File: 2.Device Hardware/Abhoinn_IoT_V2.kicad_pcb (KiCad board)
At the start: 4 copper layers, 46 parts, among them IC1 AX-SIP-SFEU-1-01-TX30, IC2 MS5840-02BA01, J1 Conn_01x02, J2 Conn_01x02, J3 Conn_02x05_Odd_Even, J4 Conn_02x05_Odd_Even, J5 Conn_Coaxial, J6 Conn_01x02_Female, P1 USB_C_Plug_USB2.0, U1 XC6206PxxxMR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

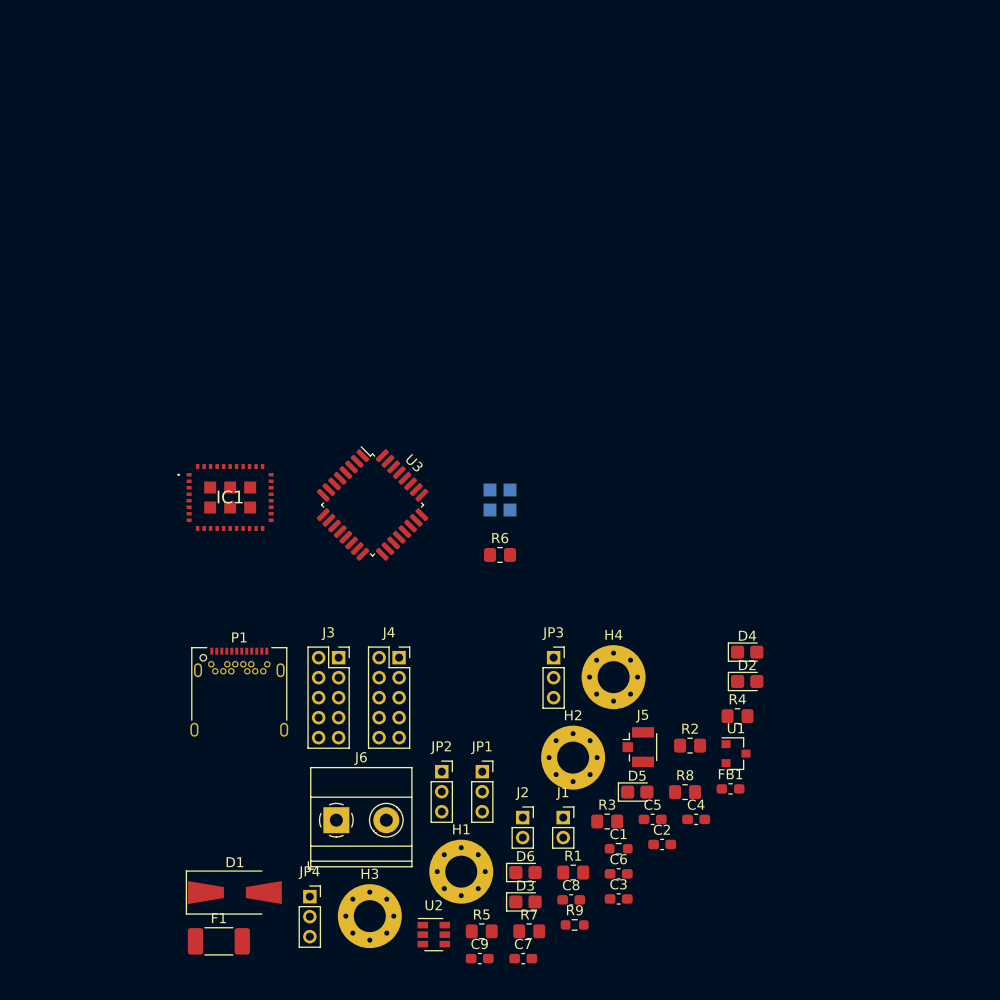
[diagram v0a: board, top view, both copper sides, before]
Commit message: Updated PCB and SCH
Updated PCB and SCH to add USB interface
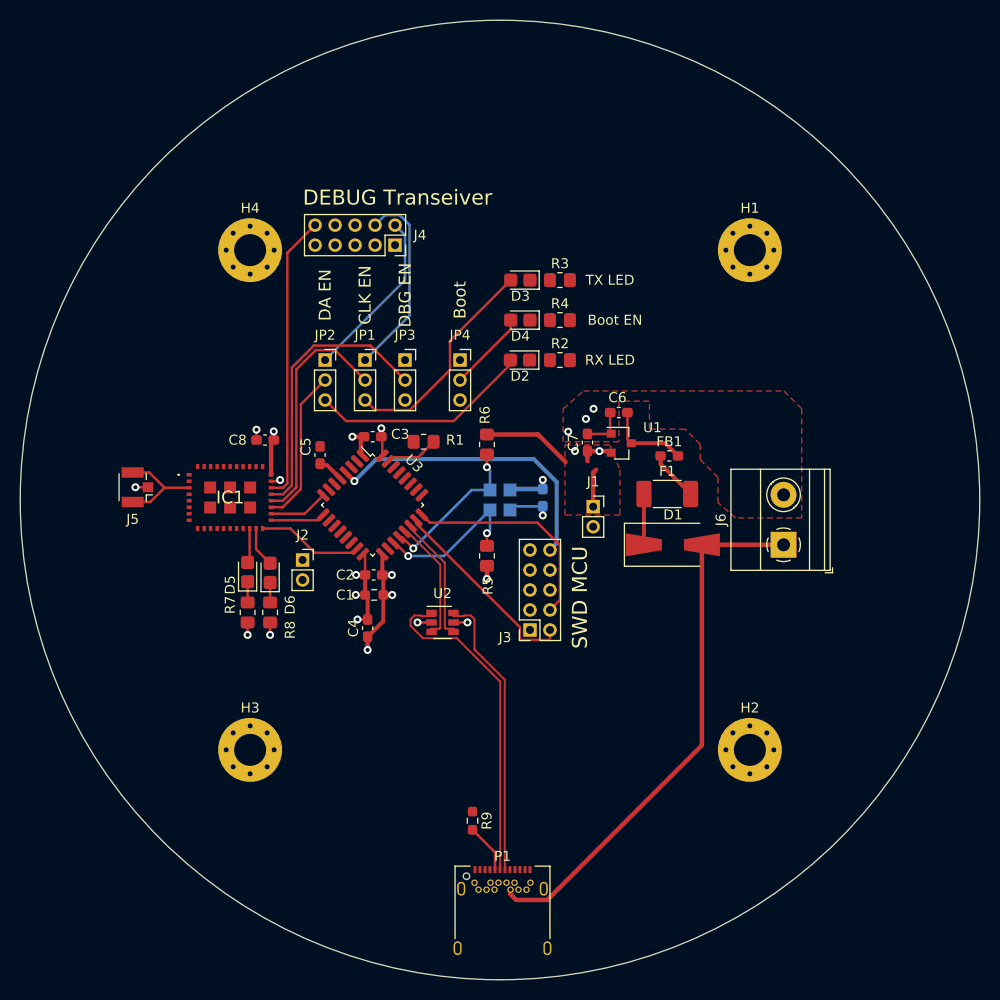
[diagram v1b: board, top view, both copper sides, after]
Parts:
- C9: moved to B.Cu
- moved H1 68.6 mm to (181.5, 55.5)
- moved F1 63.4 mm to (173.2, 79.9)
- moved D3 62.2 mm to (158.5, 58.5), turned to 180 degrees
- moved J5 56.5 mm to (120.2, 79.2), turned to 180 degrees
- moved H4 56.1 mm to (131.5, 55.5)
- moved D1 56.0 mm to (173.8, 85.0)
- moved JP4 55.7 mm to (152.5, 66.5)
- moved C8 55.3 mm to (133.0, 74.5), turned to 180 degrees
- moved R3 54.4 mm to (162.5, 58.5)
- moved J6 52.5 mm to (184.9, 85.0), turned to 90 degrees
- moved C3 52.4 mm to (143.8, 74.2)
- moved C7 52.0 mm to (165.2, 74.8), turned to 90 degrees
- moved C5 49.4 mm to (138.5, 76.0), turned to 90 degrees
- moved C9 46.6 mm to (160.8, 80.3), turned to 270 degrees
- moved C6 46.2 mm to (168.4, 71.8), turned to 180 degrees
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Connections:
- net Net-(P1-PadA6) renamed D+
- net Net-(P1-PadA7) renamed D-
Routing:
- net +5V: track 0.00 -> 54.5 mm
- net +3V3: track 0.00 -> 44.8 mm, vias 0 -> 9
- net D+: track 0.00 -> 33.8 mm
- net NRST: track 0.00 -> 30.4 mm, vias 0 -> 1
- net D-: track 0.00 -> 28.9 mm
- net RESET_N: track 0.00 -> 28.8 mm
- net DBG_EN: track 0.00 -> 27.9 mm
- net GND: track 0.00 -> 27.0 mm, vias 0 -> 13
- net TX_LED+DBG_CLK: track 0.00 -> 23.8 mm
- net LED_RX: track 0.00 -> 22.2 mm
- net LED_TX: track 0.00 -> 22.1 mm
- net SWCLK: track 0.00 -> 22.0 mm
- net SWDIO: track 0.00 -> 20.2 mm
- net TS_DBG_CLK: track 0.00 -> 19.6 mm
- net TS_DBG_DATA: track 0.00 -> 17.2 mm
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- added copper zone on F.Cu, net +3V3
- added copper zone on F.Cu, net GND
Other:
- board outline added: 96 x 96 mm
- net class POWER+ added: clearance 0.2, trace_width 0.45, via_dia 0.8, via_drill 0.4
- board text added: "Boot"
- board text added: "Boot EN"
- board text added: "CLK EN"
- board text added: "DA EN"
- board text added: "DBG EN"
- board text added: "DEBUG Transeiver"
- board text added: "RX LED"
- board text added: "SWD MCU"
- board text added: "TX LED"
